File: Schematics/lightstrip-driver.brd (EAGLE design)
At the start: 40.3 x 49.5 mm, 11 parts, among them IC1 MCP2300X/P, Q1 FQP30N06L, Q2 FQP30N06L, Q3 FQP30N06L

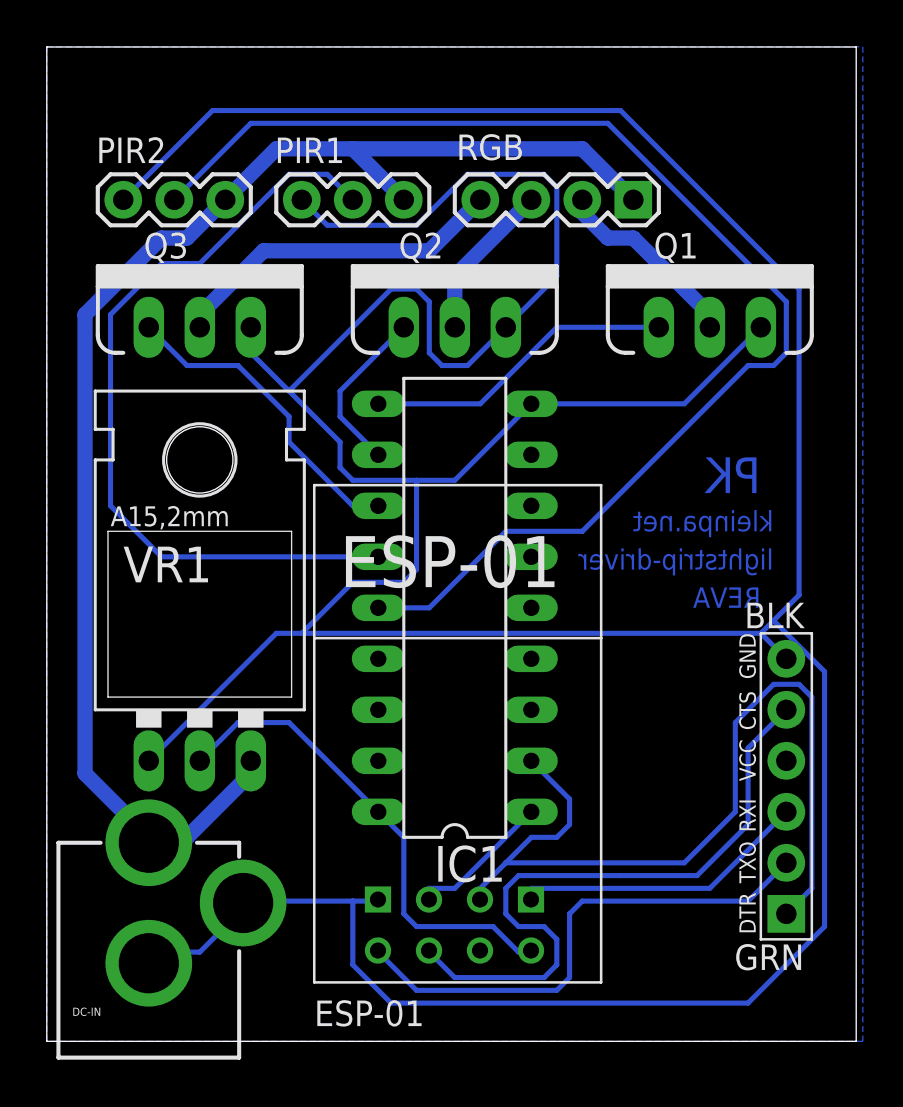
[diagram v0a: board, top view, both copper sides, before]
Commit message: Update board with correct ESP8266 autoreset connections
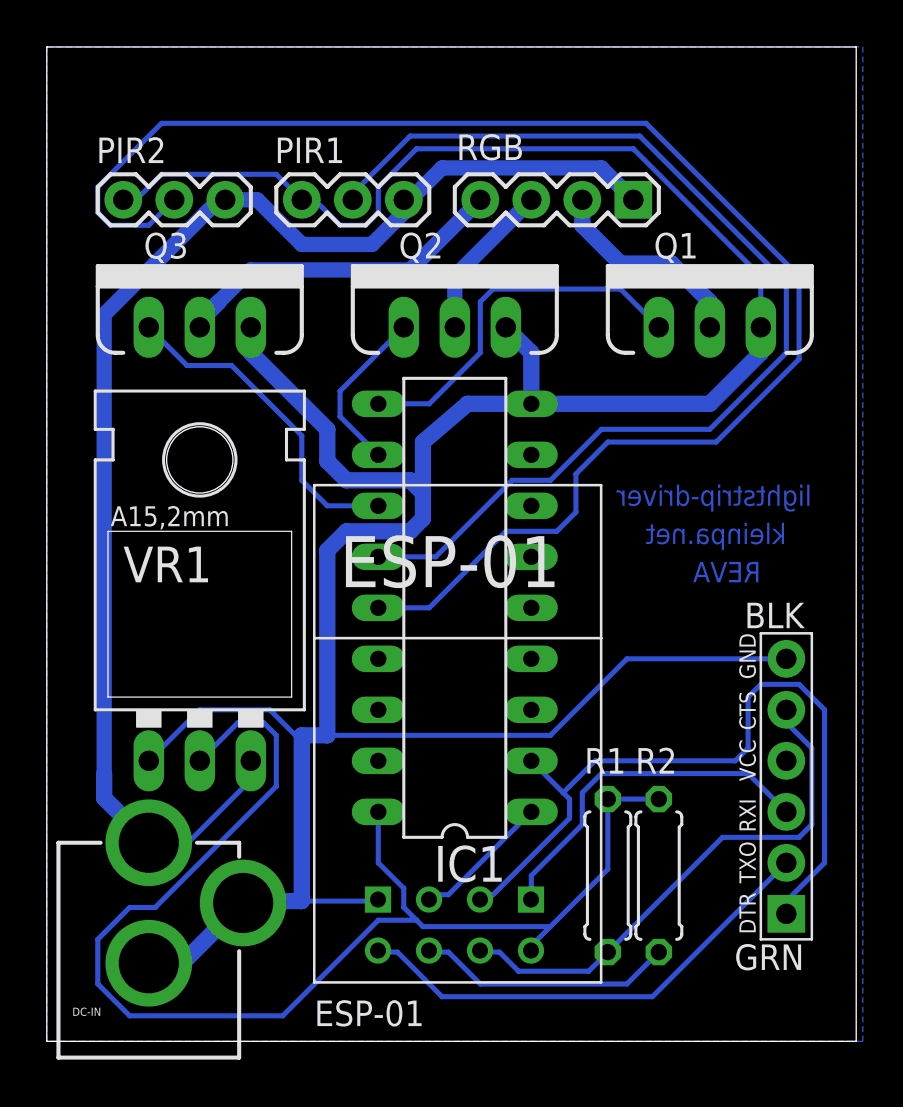
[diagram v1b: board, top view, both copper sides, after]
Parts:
- added R1, R2: 10k, resistor:0207/7
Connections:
- removed net N$10: ESP-01.CH_PD, JP1.P$5
- new net N$15: ESP-01.RST, JP1.P$5, R1.1
- new net N$3: ESP-01.CH_PD, R2.1
- net +3V3: now also R1.2, R2.2
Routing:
- net GND: track 234.5 -> 154.3 mm
- net +3V3: track 24.3 -> 64.8 mm
- net N$10: track 32.7 -> 0.00 mm
- net N$15: track 0.00 -> 26.2 mm
- net N$1: track 39.4 -> 54.1 mm
- net N$3: track 0.00 -> 12.8 mm
- net N$13: track 63.9 -> 76.6 mm
- net N$14: track 43.4 -> 38.1 mm
- net +12V: track 70.0 -> 66.8 mm
- net N$4: track 15.5 -> 18.6 mm
- net N$7: track 14.8 -> 17.7 mm
- net N$9: track 25.7 -> 24.1 mm
- net N$6: track 15.9 -> 17.0 mm
- net N$8: track 9.72 -> 10.5 mm
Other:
- board text removed: "PK"

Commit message: Add mounting holes
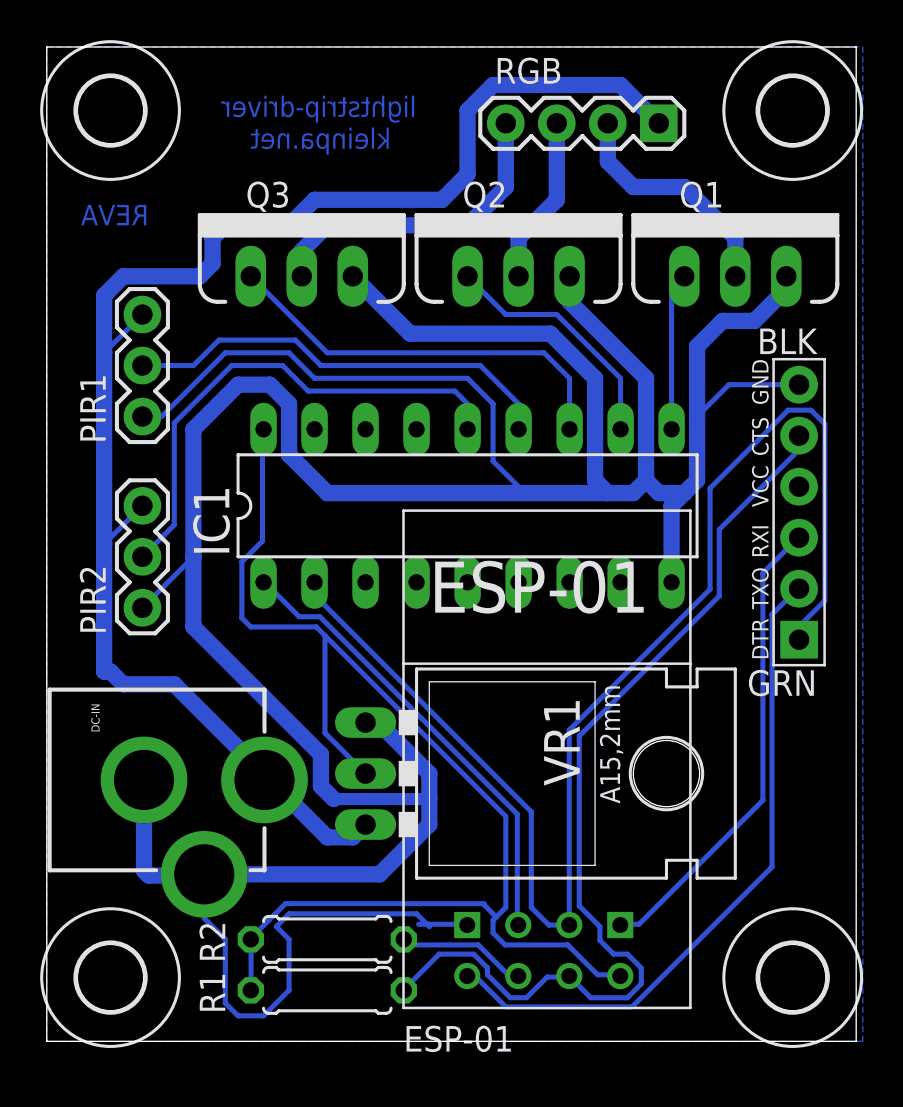
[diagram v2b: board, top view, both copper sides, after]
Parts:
- added H1, H2, H3, H4: MOUNT-HOLE3.3, holes:3,3
- moved PIR2 20.3 mm to (4.76, 21.6), turned to 90 degrees
- moved DC-IN 18.6 mm to (-2.86, 13.0), turned to 270 degrees
- moved R2 16.8 mm to (14.0, 5.08), turned to 180 degrees
- moved R1 15.1 mm to (14.0, 2.54), turned to 180 degrees
- moved JP1 13.7 mm to (37.5, 26.4)
- moved PIR1 13.4 mm to (4.76, 31.1), turned to 90 degrees
- moved VR1 12.9 mm to (19.7, 13.3), turned to 270 degrees
- moved Q3 5.68 mm to (12.7, 38.1)
- moved IC1 5.12 mm to (21.0, 26.7), turned to 0 degrees
- moved ESP-01 4.62 mm to (24.8, 11.4)
- moved Q2 4.07 mm to (23.5, 38.1)
- moved RGB 4.02 mm to (30.5, 45.7)
- moved Q1 2.84 mm to (34.3, 38.1)
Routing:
- net N$13: track 76.6 -> 25.2 mm
- net GND: track 154.3 -> 192.0 mm
- net N$1: track 54.1 -> 21.8 mm
- net N$14: track 38.1 -> 66.5 mm
- net N$15: track 26.2 -> 48.4 mm
- net N$2: track 7.03 -> 23.0 mm
- net N$4: track 18.6 -> 7.88 mm
- net +12V: track 66.8 -> 76.3 mm
- net N$9: track 24.1 -> 33.1 mm
- net N$3: track 12.8 -> 6.46 mm
- net N$7: track 17.7 -> 23.5 mm
- net N$5: track 8.45 -> 12.3 mm
- net N$6: track 17.0 -> 20.5 mm
- net N$8: track 10.5 -> 11.7 mm
- net +3V3: track 64.8 -> 63.8 mm
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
